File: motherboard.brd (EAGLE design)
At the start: 177.1 x 75.9 mm, 183 parts, among them IC1 LM2576, IC10 TUSB2046B, IC12 LM50, IC13 LM50, IC2 74LS595D, IC3 74LS595D, IC4 IC_FT230X-SSOP-16, IC5 VN5772AK, IC6 VN5772AK, IC7 VN5772AK, IC8 VN5772AK, IC9 VN5772AK, U2 NCP4625, U3 ATMEGA168, Y1 16Mhz, Y2 6MHz

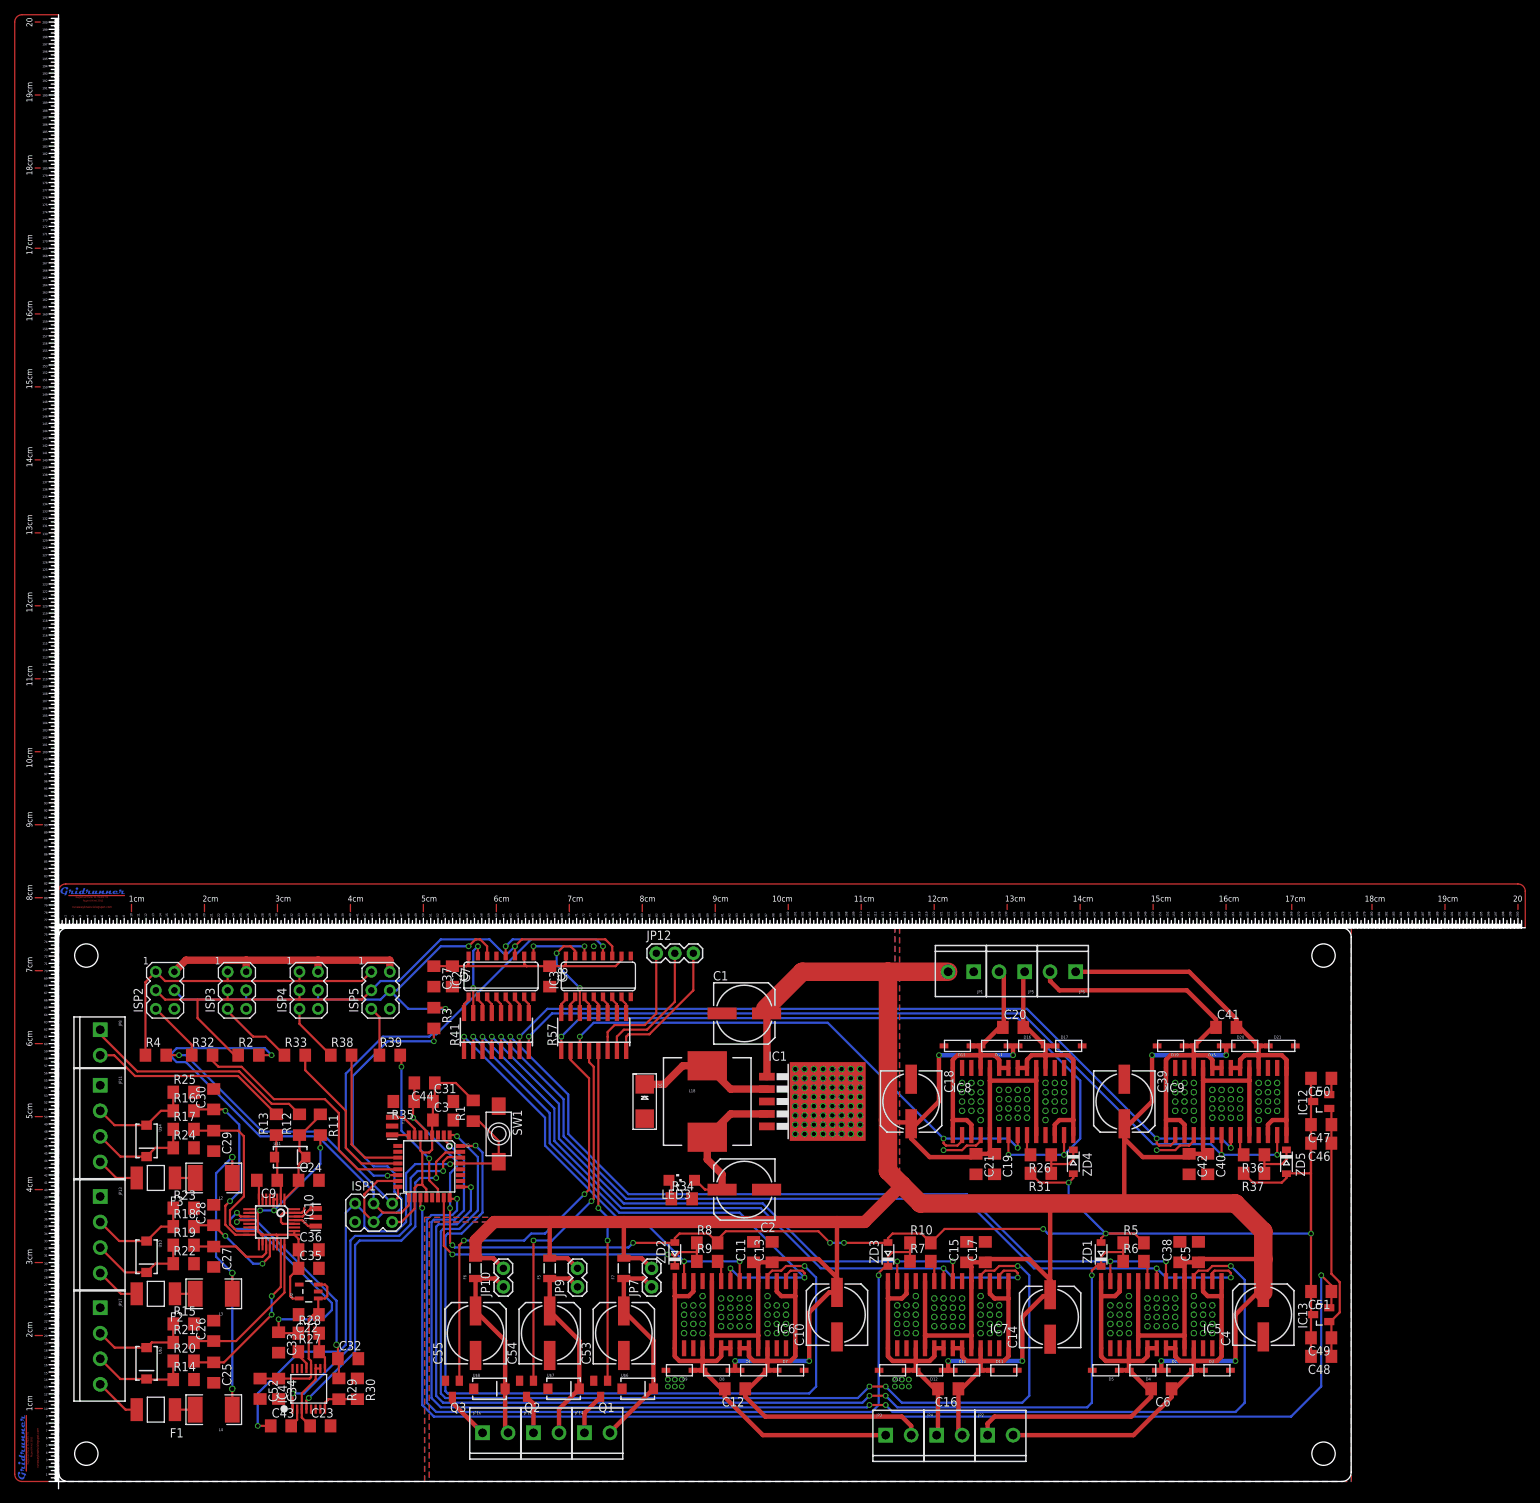
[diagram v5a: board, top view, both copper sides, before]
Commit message: finished initial routing
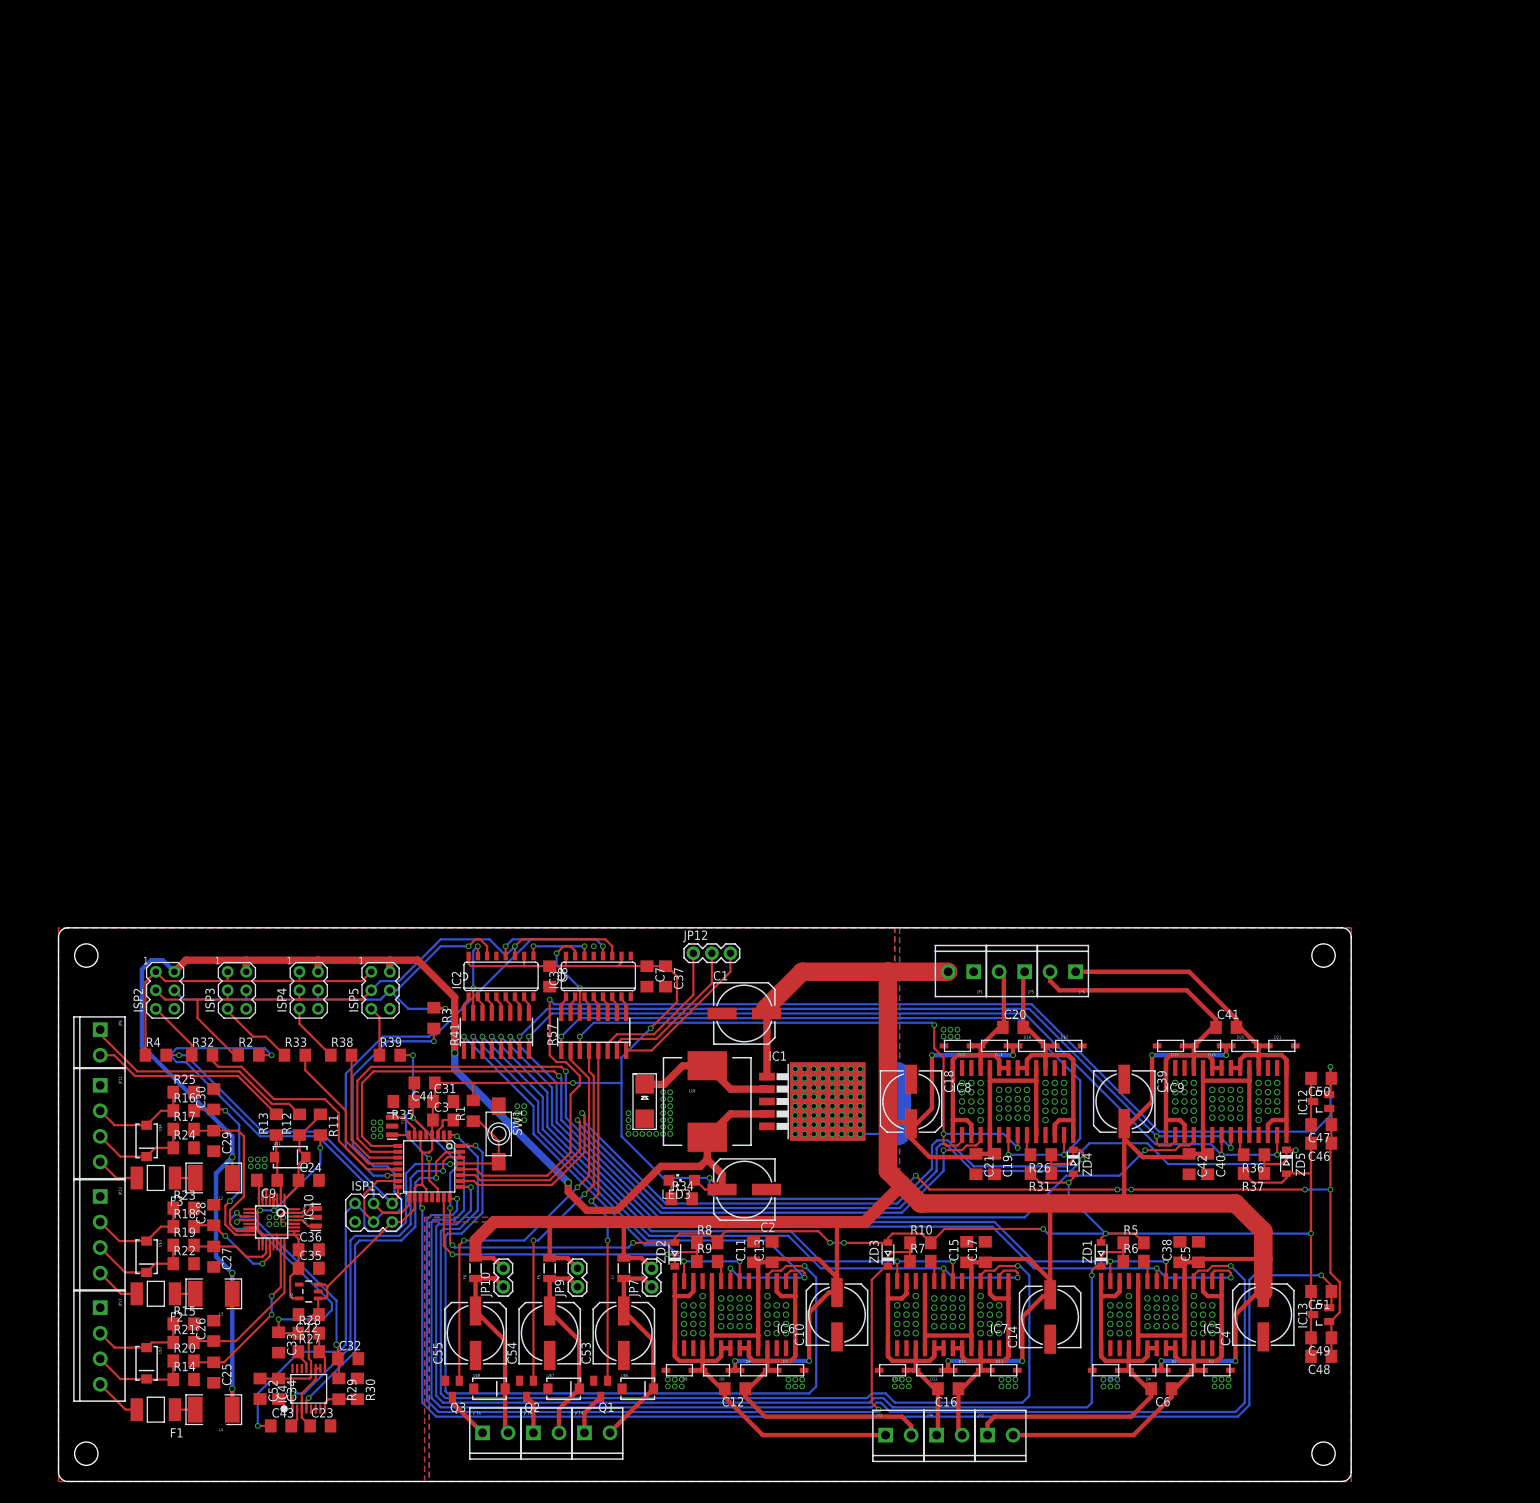
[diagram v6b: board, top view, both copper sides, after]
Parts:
- removed U$17, U$18: (no value), CAD Ruler_EagleCad Gridrunner XL Metric V1 (Rupert Hirst 2011):RULER
- moved C37 31.8 mm to (83.2, 69.2)
- moved C7 26.7 mm to (80.6, 69.2)
- moved JP12 5.08 mm to (87.0, 72.4)
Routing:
- net +5V: track 222.7 -> 495.7 mm, vias 3 -> 13
- net TEMP0: track 2.35 -> 167.1 mm, vias 0 -> 2
- net 3SENSE: track 7.14 -> 146.7 mm, vias 0 -> 2
- net 3STAT: track 6.40 -> 144.2 mm, vias 1 -> 2
- net 4STAT: track 6.40 -> 119.0 mm, vias 1 -> 2
- net 4SENSE: track 7.14 -> 114.2 mm, vias 0 -> 2
- net GND: track 12.4 -> 35.7 mm, vias 287 -> 363
- net 4HA: track 76.1 -> 84.8 mm, vias 3 -> 4
- net SW4: track 18.5 -> 21.6 mm
- net SW3: track 18.6 -> 21.2 mm
- net SW5: track 18.9 -> 21.4 mm
- net !EN1: track 21.7 -> 23.7 mm
- net SW0: track 59.6 -> 58.5 mm
- net SW1: track 50.4 -> 49.3 mm
- net 1SENSE: track 122.1 -> 123.1 mm
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
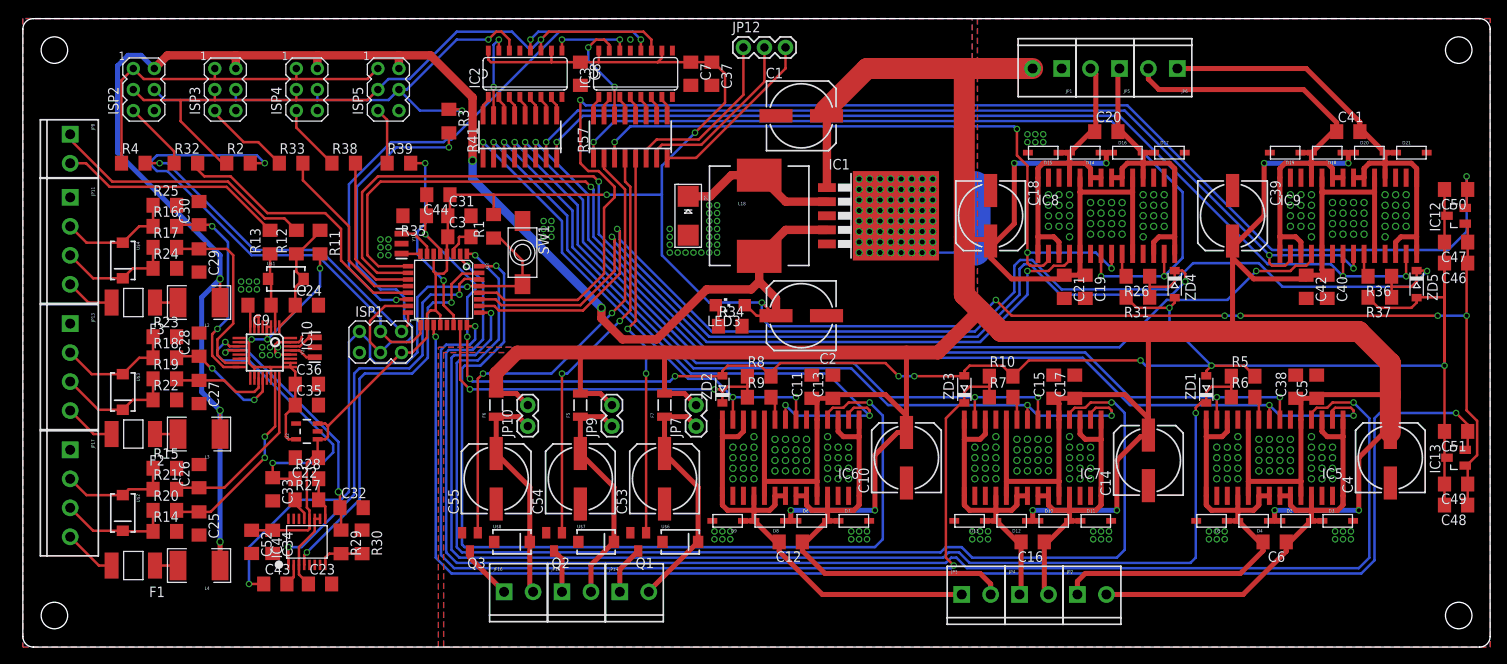
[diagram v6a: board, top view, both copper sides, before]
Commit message: finished silkscreen
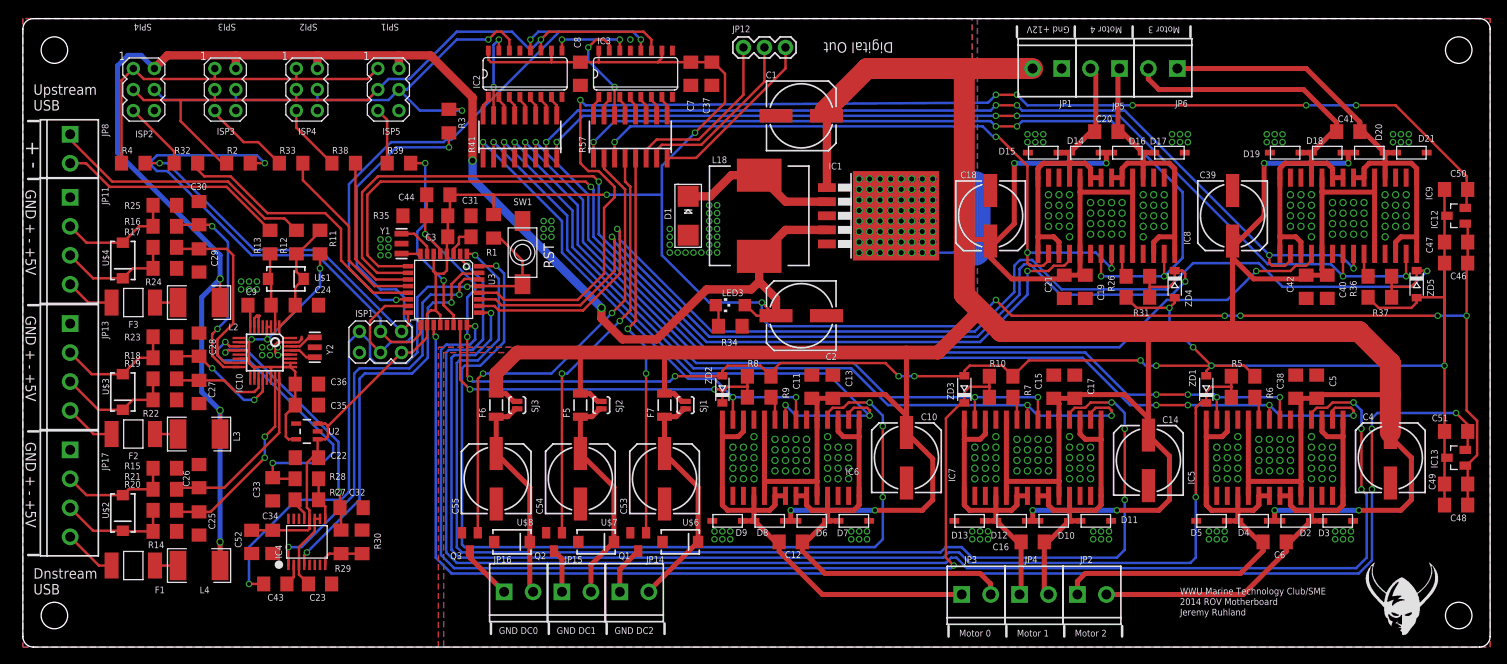
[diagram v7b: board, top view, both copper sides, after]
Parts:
- removed JP10, JP7, JP9: (no value), sparkfun:1X02
- added SJ1, SJ2, SJ3: JMP, sparkfun:SJ_2S-NO
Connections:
- net +12V: now also SJ1.2, SJ2.2, SJ3.2; no longer JP10.2, JP7.2, JP9.2
- net N$50: now also SJ3.1; no longer JP10.1
- net N$54: now also SJ2.1; no longer JP9.1
- net N$55: now also SJ1.1; no longer JP7.1
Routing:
- net +12V: track 612.8 -> 623.9 mm
- net TEMP0: track 167.1 -> 156.7 mm, vias 2 -> 6
- net 4HA: track 84.8 -> 82.9 mm
- net N$54: track 28.3 -> 26.9 mm
- net N$50: track 27.3 -> 25.9 mm
- net N$55: track 29.6 -> 28.2 mm
- net 4HB: track 101.8 -> 102.3 mm, vias 3 -> 5
- net 3HA: track 115.3 -> 115.9 mm, vias 3 -> 5
- net 2STAT: track 179.9 -> 179.5 mm, vias 2 -> 4
- net TEMP1: vias 2 -> 4
- net AGND: vias 10 -> 12
- net GND: vias 363 -> 381
- net 3HB: vias 3 -> 5
- net 2HB: vias 3 -> 5
- net 2HA: vias 3 -> 5
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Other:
- board text added: "- +"
- board text added: "2014 ROV Motherboard"
- board text added: "Digital Out"
- board text added: "Dnstream"
- board text added: "GND + - +5V"
- board text added: "GND DC0"
- board text added: "GND DC1"
- board text added: "GND DC2"
- board text added: "Gnd +12V"
- board text added: "Jeremy Ruhland"
- board text added: "Motor 0"
- board text added: "Motor 1"
- board text added: "Motor 2"
- board text added: "Motor 3"
- board text added: "Motor 4"
- board text added: "RST"
- board text added: "SPI1"
- board text added: "SPI2"
- board text added: "SPI3"
- board text added: "SPI4"
- board text added: "USB"
- board text added: "Upstream"
- board text added: "WWU Marine Technology Club/SME"
